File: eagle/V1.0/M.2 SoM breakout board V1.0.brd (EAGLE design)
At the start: 140 x 122 mm, 119 parts, among them J1 3-PIN SMD, J11 WAFER-HY2.0-4PWB, J18 PARTICLE-STUDIOS_M_SERIES_M.2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, J2 DCJ0202, J21 SIP-2, J3 SPARK_CON_30X2_SMD, J5 SCREW-HOLE-3.7, J6 M.2-SOM-BREAKOUT-BOARD-V0.2-0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, J7 SCREW-HOLE-3.7, Q1 L2N7002, Q2 SI2333DS, Q3 SI2333DS, Q4 SI2333DS, Q5 SI2333DS, U1 XC8107, X1 BU-SMA-G, X2 BU-SMA-G, X3 BU-SMA-G, X4 S8111-46R, X5 S8111-46R, X6 S8111-46R

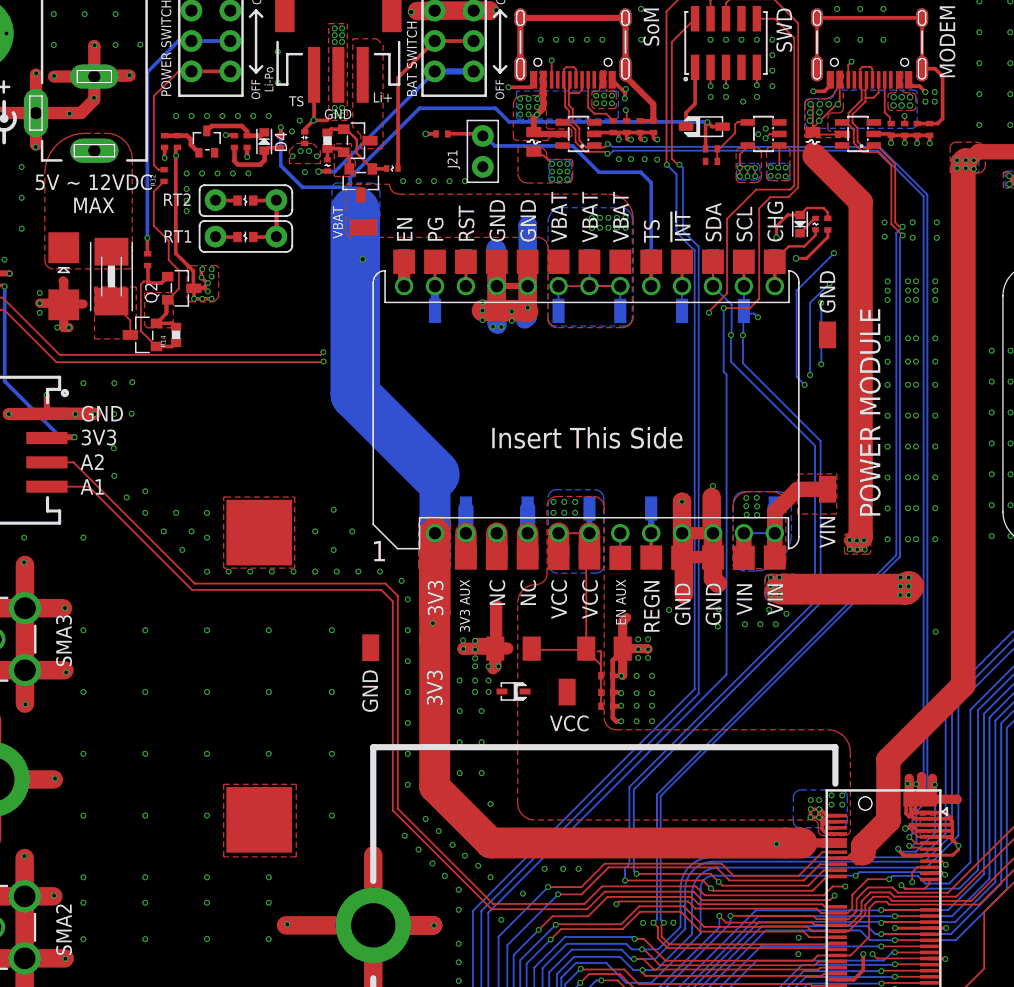
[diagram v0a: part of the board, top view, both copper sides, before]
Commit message: Please refer to change list
8.Change J6 PCB package,change drill from 1.016mm to 1.3mm. Smaller pad 0.5mm.
9.Add silkscreen label on the PCB to note that USB is only for comms and not power--"DATA ONLY"
10.Add 3V3_AUX LED.
11.Change PCB version to V1.0.
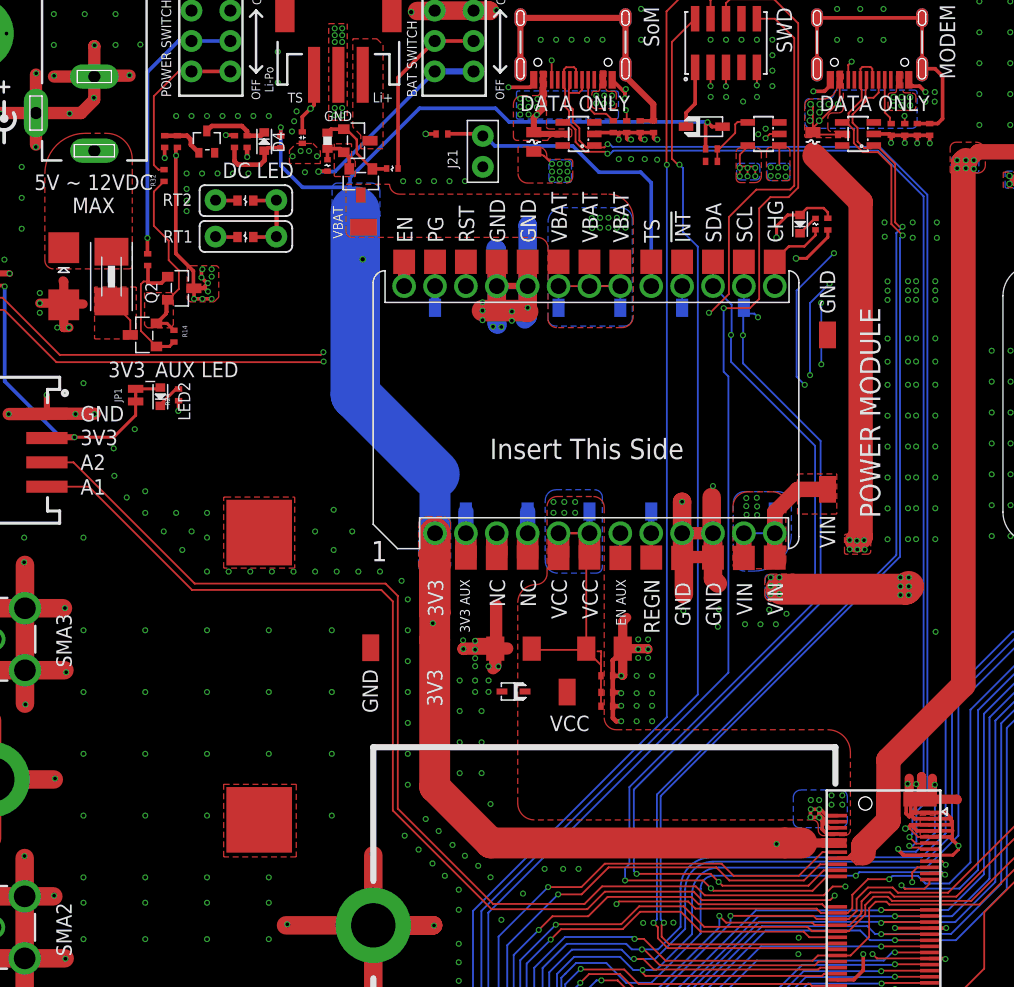
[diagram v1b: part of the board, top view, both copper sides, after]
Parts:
- added JP1: JUMPER-SMT_2_NC_TRACE_NO-SILK, SparkFun-Jumpers:SMT-JUMPER_2_NC_TRACE_NO-SILK
- added LED2: RED, particle SZ:LED0603
- added R24: 0R, Particle:R0402_B
- J6: value M.2-SOM-BREAKOUT-BOARD-V0.2-0228_PARTICLE-SZ_PARTICLE-POWER-MODULE -> M.2-SOM-BREAKOUT-BOARD-V0.3_M.2-SOM-BREAKOUT-BOARD-V0.2-0228_PARTICLE-SZ_PARTICLE-POWER-MODULE; device M.2 SoM breakout board v0.3:M.2-SOM-BREAKOUT-BOARD-V0.2-0228_PARTICLE-SZ_PARTICLE-POWER-MODULE -> M.2 SoM breakout board:M.2-SOM-BREAKOUT-BOARD-V0.3_M.2-SOM-BREAKOUT-BOARD-V0.2-0228_PARTICLE-SZ_PARTICLE-POWER-MODULE
- Q1: value L2N7002 -> DNP/L2N7002
- R14: device particle-studios:R0603_P -> Particle:R0402_B
- moved R14 0.20 mm to (20.2, 93.1), turned to 270 degrees
- moved D4 0.20 mm to (30.7, 109.4)
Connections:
- new net N$14: LED2.2, R24.2
- new net N$47: JP1.2, LED2.1
- net 3V3_AUX: now also JP1.1
- net GND: now also R24.1
- net N$10: now also R14.1; no longer R14.2
- net N$17: now also R14.2; no longer R14.1
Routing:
- net 3V3_AUX: track 286.5 -> 293.1 mm
- net N$14: track 0.00 -> 2.13 mm
- net N$47: track 0.00 -> 2.07 mm
- net SWCLK: track 116.0 -> 114.1 mm
- net N$44: track 4.06 -> 5.60 mm
- net GPIO1: track 123.4 -> 124.9 mm
- net VBAT: track 63.2 -> 62.4 mm
- net VIN: track 42.2 -> 41.5 mm
- net +3V3: track 339.2 -> 338.7 mm
- net GND: track 668.5 -> 668.6 mm, vias 744 -> 743
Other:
- board text added: "3V3_AUX LED"
- board text added: "DATA ONLY"
- board text added: "DC LED"
- board text added: "USB FOR DATA ONLY"
- board text removed: "SIP-3"

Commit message: Move Q2 position.
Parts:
- Q2, Q3, Q4, Q5: value SI2333DS -> SI2333DDS
- R24: value 0R -> 1K
- moved Q2 0.92 mm to (18.5, 93.7)
- moved R14 0.77 mm to (20.9, 93.2)
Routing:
- net N$10: track 18.2 -> 16.4 mm
- net N$17: track 11.2 -> 10.2 mm

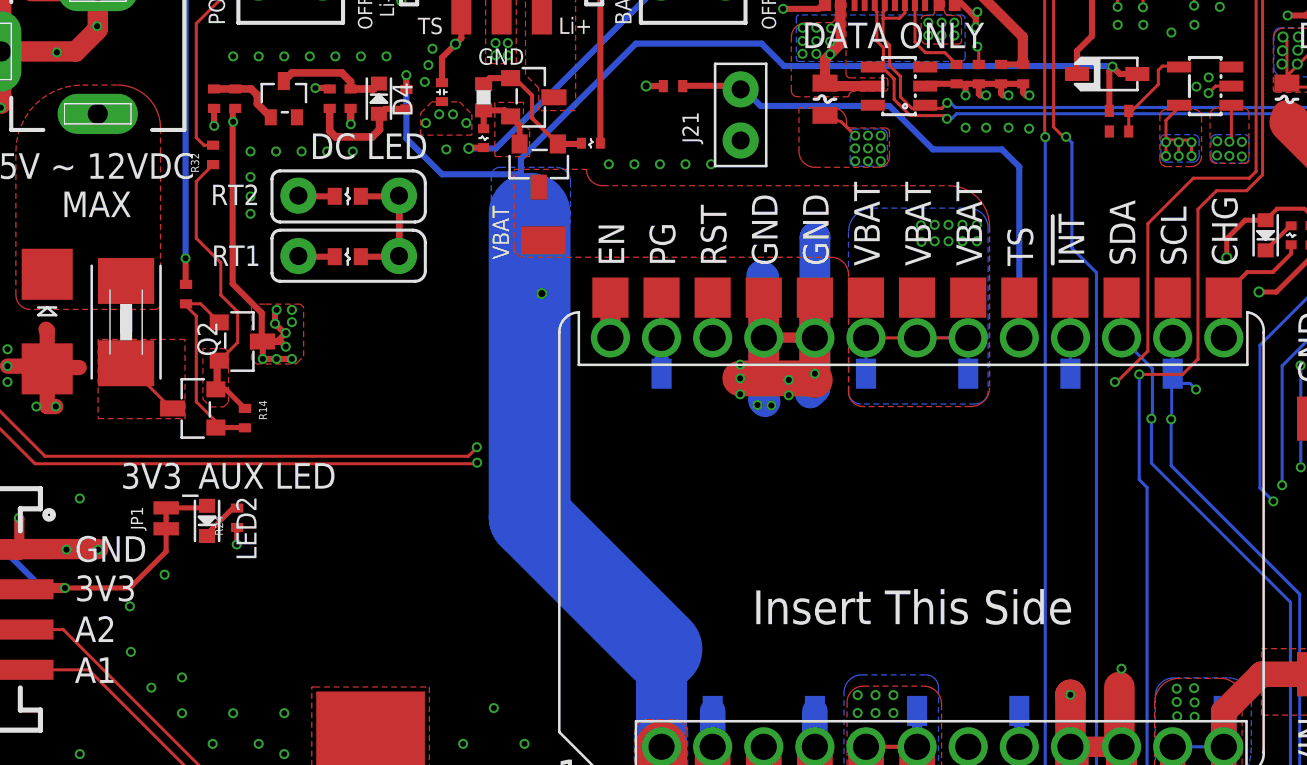
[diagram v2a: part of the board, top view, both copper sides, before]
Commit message: updated label text and logo on the bottom
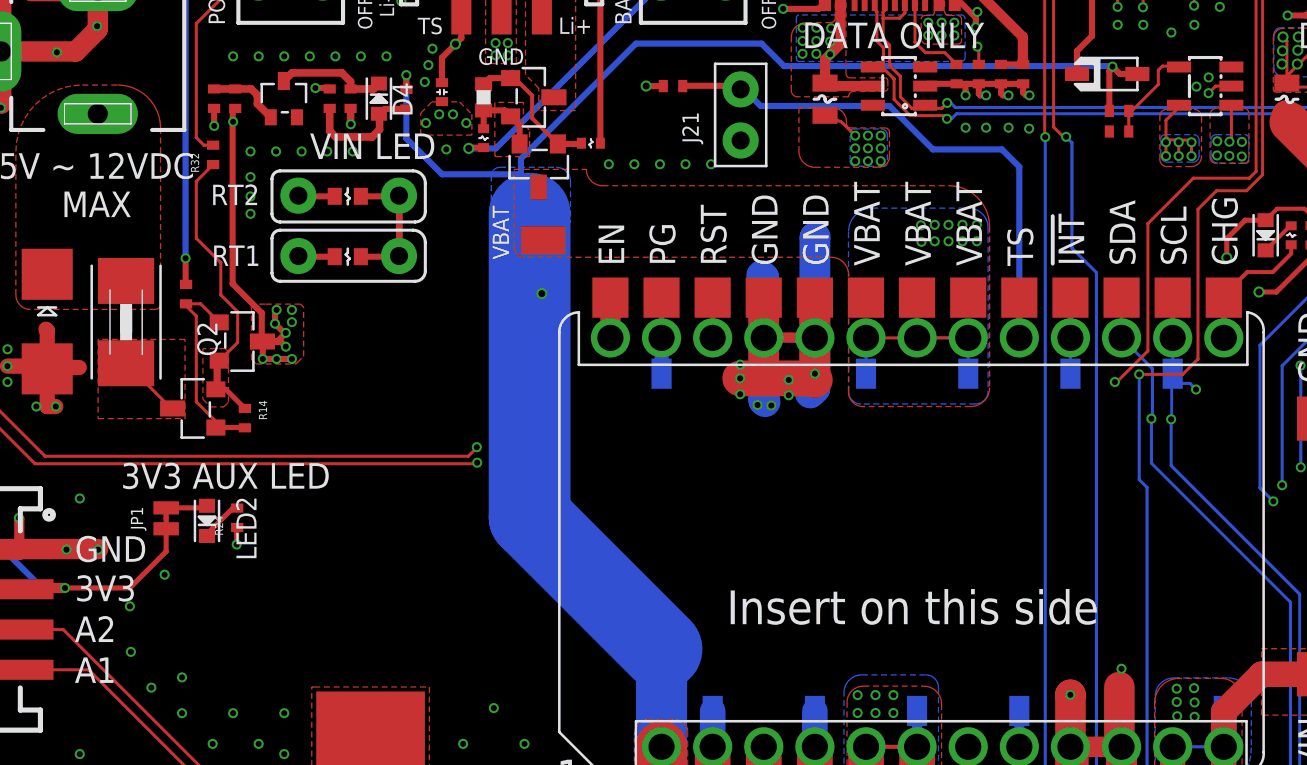
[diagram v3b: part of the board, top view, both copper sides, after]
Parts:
- removed U$6: PARTICLE-LOGO, particle SZ:PARTICLE-LOGO
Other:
- board text added: "3V3 AUX LED"
- board text added: "Insert on this side"
- board text added: "Power Module - Insert on top side"
- board text added: "VIN LED"
- board text removed: "3V3_AUX LED"
- board text removed: "DC LED"
- board text removed: "Insert This Side"
- board text removed: "Power Module - Insert on Top Side"
